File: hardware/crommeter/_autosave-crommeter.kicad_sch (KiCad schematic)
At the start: 52 parts, among them J1 10118194-0001LF, J2 Conn_01x03_Pin, J3 PRT-14417, P1 S2B-PH-SM4-TB, Q1 BSD840NH6327XTSA1, Q2 BSD840NH6327XTSA1, Q3 BSD840NH6327XTSA1, SW1 SW_Push_Dual, U1 RP2350_Stamp, U2 Common Cathode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

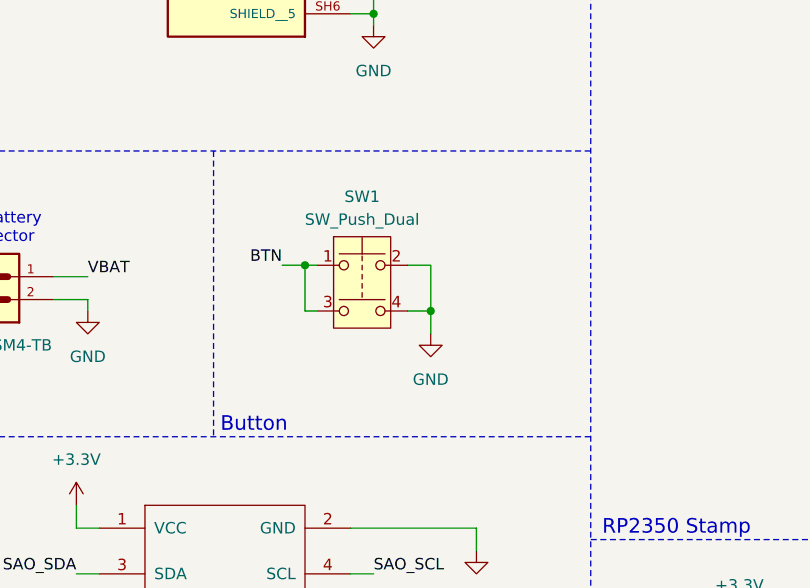
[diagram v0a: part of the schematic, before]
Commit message: Finished schematic. Parts placed in general areas.
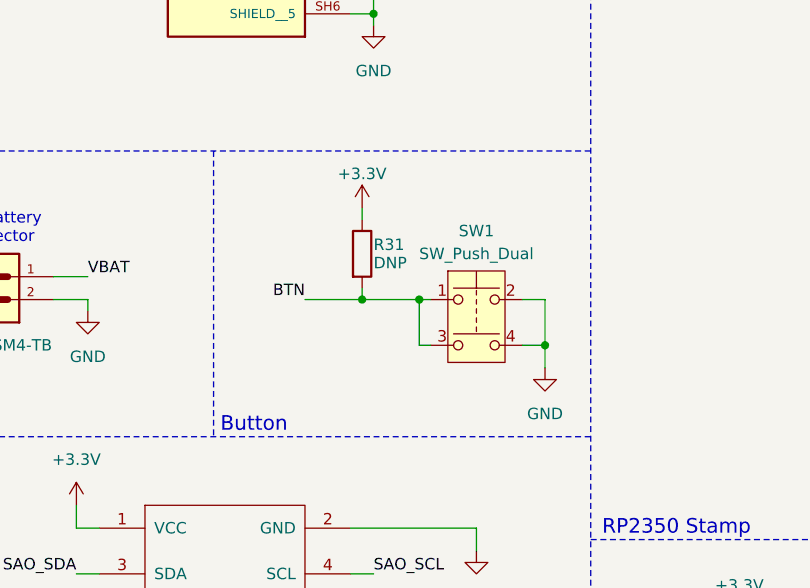
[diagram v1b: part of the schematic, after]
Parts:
- added R31: DNP, Resistor_SMD:R_0603_1608Metric_Pad0.98x0.95mm_HandSolder, symbol Device:R
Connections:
- net +3.3V: now also R31.1
- net BTN: now also R31.2
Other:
- moved on the sheet: SW1
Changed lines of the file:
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@@
 	)
 	(junction
+		(at 64.77 91.44)
+		(diameter 0)
+		(color 0 0 0 0)
+	)
+	(junction
 		(at 234.95 149.86)
 		(diameter 0)
@@
 	)
 	(junction
-		(at 58.42 87.63)
+		(at 71.12 91.44)
 		(diameter 0)
 		(color 0 0 0 0)
@@
 	)
 	(junction
-		(at 72.39 92.71)
+		(at 85.09 96.52)
 		(diameter 0)
 		(color 0 0 0 0)
@@
 	(wire
 		(pts
-			(xy 59.69 92.71) (xy 58.42 92.71)
+			(xy 72.39 96.52) (xy 71.12 96.52)
 		)
 		(stroke
@@
 	(wire
 		(pts
-			(xy 55.88 87.63) (xy 58.42 87.63)
-		)
-		(stroke
-			(width 0)
-			(type default)
-		)
-	)
-	(wire
-		(pts
 			(xy 146.05 69.85) (xy 148.59 69.85)
 		)
@@
 	(wire
 		(pts
-			(xy 69.85 87.63) (xy 72.39 87.63)
+			(xy 82.55 91.44) (xy 85.09 91.44)
 		)
 		(stroke
@@
 	(wire
 		(pts
-			(xy 72.39 87.63) (xy 72.39 92.71)
+			(xy 85.09 91.44) (xy 85.09 96.52)
 		)
 		(stroke
@@
 	(wire
 		(pts
+			(xy 64.77 81.28) (xy 64.77 82.55)
+		)
+		(stroke
+			(width 0)
+			(type default)
+		)
+	)
+	(wire
+		(pts
 			(xy 210.82 46.99) (xy 226.06 46.99)
 		)
@@
 	(wire
 		(pts
+			(xy 64.77 90.17) (xy 64.77 91.44)
+		)
+		(stroke
+			(width 0)
+			(type default)
+		)
+	)
+	(wire
+		(pts
 			(xy 261.62 119.38) (xy 261.62 110.49)
 		)
@@
 	(wire
 		(pts
-			(xy 58.42 92.71) (xy 58.42 87.63)
+			(xy 71.12 96.52) (xy 71.12 91.44)
 		)
 		(stroke
@@
 	(wire
 		(pts
-			(xy 72.39 92.71) (xy 72.39 95.25)
+			(xy 85.09 96.52) (xy 85.09 99.06)
 		)
 		(stroke
@@
 	(wire
 		(pts
+			(xy 64.77 91.44) (xy 71.12 91.44)
+		)
+		(stroke
+			(width 0)
+			(type default)
+		)
+	)
+	(wire
+		(pts
 			(xy 40.64 146.05) (xy 40.64 147.32)
 		)
@@
 	(wire
 		(pts
+			(xy 58.42 91.44) (xy 64.77 91.44)
+		)
+		(stroke
+			(width 0)
+			(type default)
+		)
+	)
+	(wire
+		(pts
 			(xy 66.04 52.07) (xy 66.04 54.61)
 		)
@@
 	(wire
 		(pts
-			(xy 58.42 87.63) (xy 59.69 87.63)
+			(xy 71.12 91.44) (xy 72.39 91.44)
 		)
 		(stroke
@@
 	(wire
 		(pts
-			(xy 69.85 92.71) (xy 72.39 92.71)
+			(xy 82.55 96.52) (xy 85.09 96.52)
 		)
 		(stroke
@@
 	)
 	(label "BTN"
-		(at 55.88 87.63 180)
+		(at 58.42 91.44 180)
 		(effects
 			(font
@@
 	(symbol
 		(lib_id "Device:R")
+		(at 64.77 86.36 0)
+		(unit 1)
+		(exclude_from_sim no)
+		(in_bom yes)
+		(on_board yes)
+		(dnp no)
+		(property "Reference" "R31"
+			(at 66.04 85.344 0)
+			(effects
+				(font
+					(size 1.27 1.27)
+				)
+				(justify left)
+			)
+		)
+		(property "Value" "DNP"
+			(at 66.04 87.376 0)
+			(effects
+				(font
+					(size 1.27 1.27)
+				)
+				(justify left)
+			)
+		)
+		(property "Footprint" "Resistor_SMD:R_0603_1608Metric_Pad0.98x0.95mm_HandSolder"
+			(at 62.992 86.36 90)
+			(effects
+				(font
+					(size 1.27 1.27)
+				)
+				(hide yes)
+			)
+		)
+		(property "Datasheet" "~"
+			(at 64.77 86.36 0)
+			(effects
+				(font
+					(size 1.27 1.27)
+				)
+				(hide yes)
+			)
+		)
+		(property "Description" "Resistor"
+			(at 64.77 86.36 0)
+			(effects
+				(font
+					(size 1.27 1.27)
+				)
+				(hide yes)
+			)
+		)
+		(pin "2"
+		)
+		(pin "1"
+		)
+		(instances
+			(project "crommeter"
+				(path "/5f645a1a-176f-4a66-add3-9e2d767f9aed"
+					(reference "R31")
+					(unit 1)
+				)
+			)
+		)
+	)
+	(symbol
+		(lib_id "Device:R")
 		(at 204.47 57.15 90)
 		(unit 1)
@@
 	(symbol
 		(lib_id "power:+3.3V")
+		(at 64.77 81.28 0)
+		(unit 1)
+		(exclude_from_sim no)
+		(in_bom yes)
+		(on_board yes)
+		(dnp no)
+		(property "Reference" "#PWR026"
+			(at 64.77 85.09 0)
+			(effects
+				(font
+					(size 1.27 1.27)
+				)
+				(hide yes)
+			)
+		)
+		(property "Value" "+3.3V"
+			(at 64.77 77.47 0)
+			(effects
+				(font
+					(size 1.27 1.27)
+				)
+			)
+		)
+		(property "Footprint" ""
+			(at 64.77 81.28 0)
+			(effects
+				(font
+					(size 1.27 1.27)
+				)
+				(hide yes)
+			)
+		)
+		(property "Datasheet" ""
+			(at 64.77 81.28 0)
+			(effects
+				(font
+					(size 1.27 1.27)
+				)
+				(hide yes)
+			)
+		)
+		(property "Description" "Power symbol creates a global label with name \"+3.3V\""
+			(at 64.77 81.28 0)
+			(effects
+				(font
+					(size 1.27 1.27)
+				)
+				(hide yes)
+			)
+		)
+		(pin "1"
+		)
+		(instances
+			(project "crommeter"
+				(path "/5f645a1a-176f-4a66-add3-9e2d767f9aed"
+					(reference "#PWR026")
+					(unit 1)
+				)
+			)
+		)
+	)
+	(symbol
+		(lib_id "power:+3.3V")
 		(at 256.54 135.89 0)
 		(unit 1)
@@
 	(symbol
 		(lib_id "power:GND")
-		(at 72.39 95.25 0)
+		(at 85.09 99.06 0)
 		(unit 1)
 		(exclude_from_sim no)
@@
 		(fields_autoplaced yes)
 		(property "Reference" "#PWR013"
-			(at 72.39 101.6 0)
+			(at 85.09 105.41 0)
 			(effects
 				(font
@@
 		)
 		(property "Value" "GND"
-			(at 72.39 100.33 0)
+			(at 85.09 104.14 0)
 			(effects
 				(font
@@
 		)
 		(property "Footprint" ""
-			(at 72.39 95.25 0)
+			(at 85.09 99.06 0)
 			(effects
 				(font
@@
 		)
 		(property "Datasheet" ""
-			(at 72.39 95.25 0)
+			(at 85.09 99.06 0)
 			(effects
 				(font
@@
 		)
 		(property "Description" "Power symbol creates a global label with name \"GND\" , ground"
-			(at 72.39 95.25 0)
+			(at 85.09 99.06 0)
 			(effects
 				(font
@@
 	(symbol
 		(lib_id "Switch:SW_Push_Dual")
-		(at 64.77 90.17 0)
+		(at 77.47 93.98 0)
 		(unit 1)
 		(exclude_from_sim no)
@@
 		(fields_autoplaced yes)
 		(property "Reference" "SW1"
-			(at 64.77 80.01 0)
+			(at 77.47 83.82 0)
 			(effects
 				(font
@@
 		)
 		(property "Value" "SW_Push_Dual"
-			(at 64.77 82.55 0)
+			(at 77.47 86.36 0)
 			(effects
 				(font
@@
 		)
 		(property "Footprint" "FSM2JSMAATR:SWITCH_FSM2JSMAA_TYC"
-			(at 64.77 82.55 0)
+			(at 77.47 86.36 0)
 			(effects
 				(font
@@
 		)
 		(property "Datasheet" "~"
-			(at 64.77 90.17 0)
+			(at 77.47 93.98 0)
 			(effects
 				(font
@@
 		)
 		(property "Description" "Push button switch, generic, symbol, four pins"
-			(at 64.77 90.17 0)
+			(at 77.47 93.98 0)
 			(effects
 				(font
